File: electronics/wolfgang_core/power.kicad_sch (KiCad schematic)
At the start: 78 parts, among them J1 Power Supply, J2 Battery, J3 VXO7803-500-M-TR / ROF-78E3.3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, J4 VXO7805-500-M-TR / ROF-78E5.0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, Q1 SUM110P06-08L-E3, Q2 SUM110P06-08L-E3, Q3 SUM110P06-08L-E3, Q4 SUM110P06-08L-E3, Q5 BSS138P,215, Q6 IPD068P03L3GATMA1, SW1 power_switch, U1 LM5001MA, U2 ACS724xLCTR-50AB, U3 LTC4418IUF-PBF, U4 SN74AHCT1G08

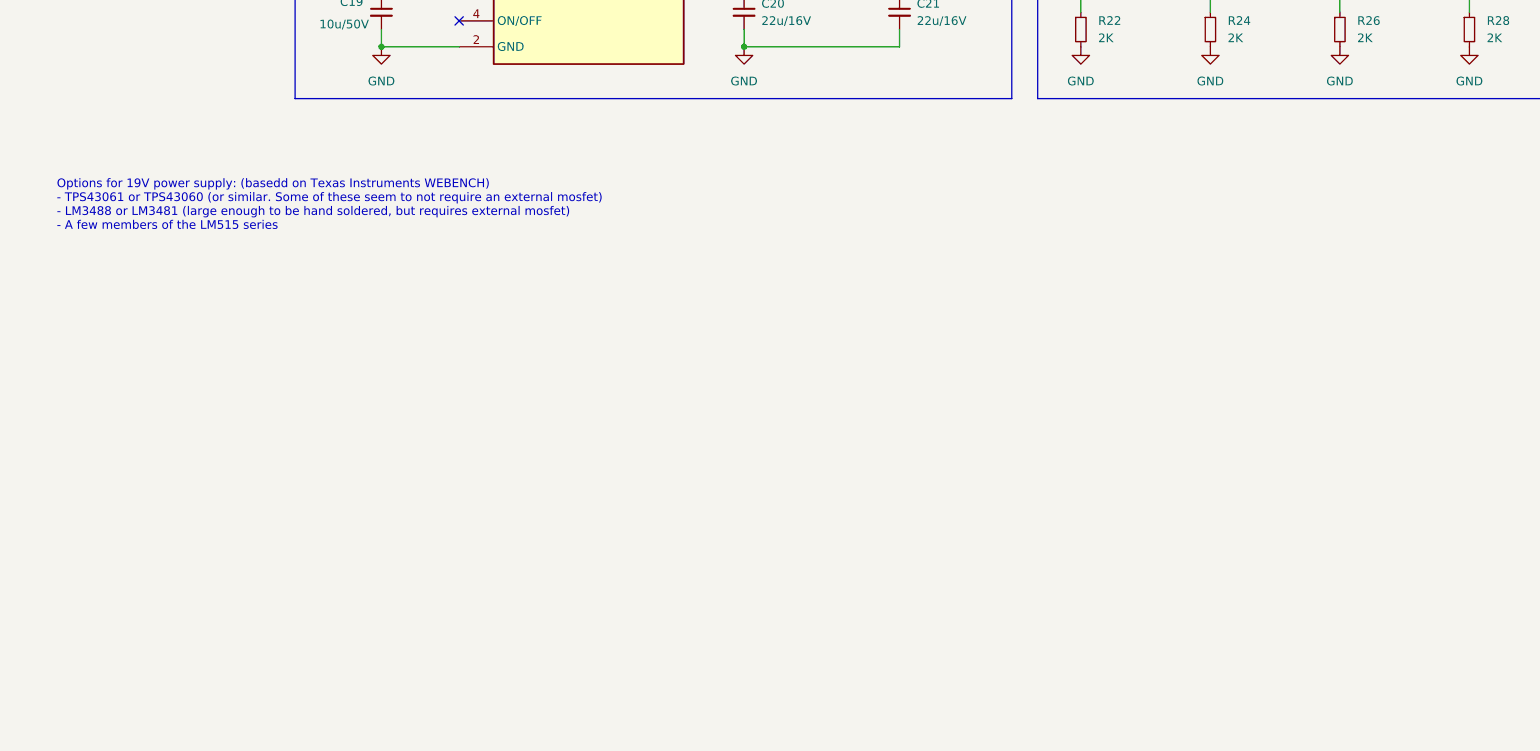
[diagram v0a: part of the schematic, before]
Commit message: Add starting point for 19V power supply
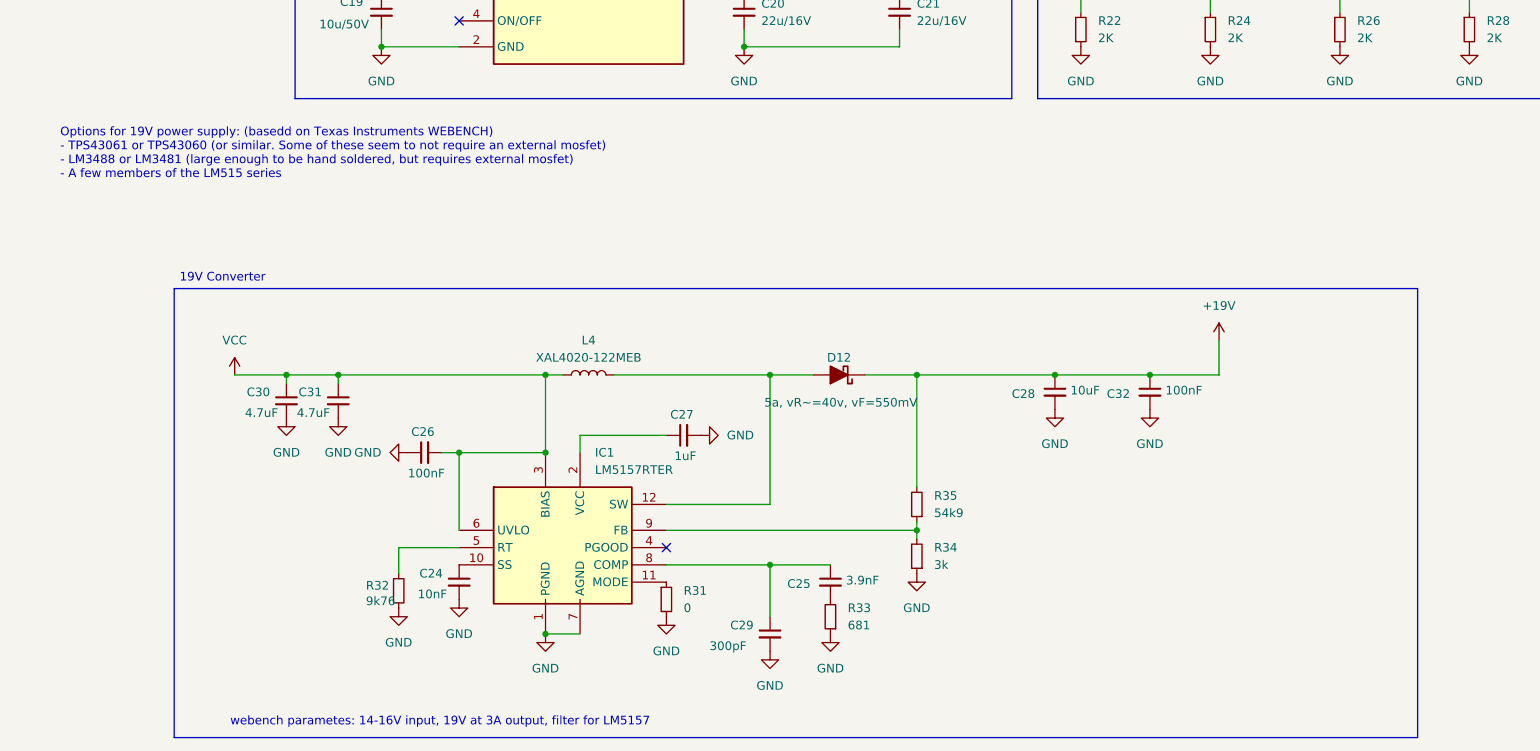
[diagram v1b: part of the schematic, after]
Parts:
- added C24: 10nF, symbol Device:C_Small
- added C25: 3.9nF, symbol Device:C_Small
- added C26, C32: 100nF, symbol Device:C_Small
- added C27: 1uF, symbol Device:C_Small
- added C28: 10uF, symbol Device:C_Small
- added C29: 300pF, symbol Device:C_Small
- added C30, C31: 4.7uF, symbol Device:C_Small
- added D12: 5a, vR~=40v, vF=550mV, symbol Device:D_Schottky_Filled
- added IC1: LM5157RTER, QFN50P300X300X80-17N-D, symbol LM5157RTER:LM5157RTER
- added L4: XAL4020-122MEB, symbol Device:L
- added R31: 0, symbol Device:R_Small
- added R32: 9k76, symbol Device:R_Small
- added R33: 681, symbol Device:R_Small
- added R34: 3k, symbol Device:R_Small
- added R35: 54k9, symbol Device:R_Small
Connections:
- net GND: now also C24.2, C26.1, C27.2, C28.2, C29.2, C30.2, C31.2, C32.2, IC1.1 (PGND), IC1.7 (AGND), R31.2, R32.2, R33.1, R34.1
- net VCC: now also C26.2, C30.1, C31.1, IC1.3 (BIAS), IC1.6 (UVLO), L4.1
- new net: IC1.5 (RT), R32.1
- new net: IC1.11 (MODE), R31.1
- new net: C24.1, IC1.10 (SS)
- new net: D12.2 (A), IC1.12 (SW), L4.2
- new net: C27.1, IC1.2 (VCC)
- new net: C25.1, C29.1, IC1.8 (COMP)
- new net: IC1.9 (FB), R34.2, R35.1
- new net: C25.2, R33.2
- new net +19V: C28.1, C32.1, D12.1 (K), R35.2
- no-connect marks 5 -> 6
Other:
- note added: "19V Converter"
- note added: "webench parametes: 14-16V input, 19V at 3A output, filter for LM5157"
